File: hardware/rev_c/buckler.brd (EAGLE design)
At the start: 63.5 x 114.3 mm, 91 parts, among them J1 DB25_5747846, J2 DM3AT-SF-PEJM5, J7 NRF52832DK_SHIELD, U1 ADXL327, U2 MAX44009, U3 MPU-9250, U4 MS5637-02BA03, U5 SI7021-A20-GM1, U6 SIP32510

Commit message: Use actual parts instead of test points
Name nrf52dk headers too.
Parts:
- removed TP1, TP10, TP11, TP12, TP13, TP14, TP15, TP16, TP17, TP18, TP19, TP2, TP20, TP21, TP22, TP23, TP24, TP25, TP26, TP27, TP28, TP29, TP3, TP30, TP31, TP32, TP33, TP34, TP39, TP4, TP5, TP6, TP7, TP8, TP9: TEST_POINT_0.040IN, headers:TESTPOINT_0.040IN
- added JP1: (no value), SparkFun-Connectors:1X02
- added JP2: (no value), SparkFun-Connectors:1X04
- added JP3: (no value), SparkFun-Connectors:1X06
- added JP4: (no value), SparkFun-Connectors:1X08
- added JP5: M10", SparkFun-Connectors:1X10
- added JP6: (no value), SparkFun-Connectors:1X05
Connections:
- net !BUTTON_0: now also JP3.4; no longer TP26.TESTPOINT
- net !IMU_INTERRUPT: now also JP6.4; no longer TP1.TESTPOINT
- net !LCD_CS: now also JP4.8; no longer TP3.TESTPOINT
- net !LED_0: now also JP5.5; no longer TP5.TESTPOINT
- net !LED_1: now also JP5.6; no longer TP6.TESTPOINT
- net !LED_2: now also JP5.7; no longer TP7.TESTPOINT
- net !LIGHT_INTERRUPT: now also JP5.1; no longer TP2.TESTPOINT
- net !RESET: now also JP6.1; no longer TP39.TESTPOINT
- net !SD_CS: now also JP4.4; no longer TP4.TESTPOINT
- net +3V3: now also JP1.1, JP1.2, JP2.4; no longer TP28.TESTPOINT, TP29.TESTPOINT, TP30.TESTPOINT
- net +5V: now also JP2.3; no longer TP31.TESTPOINT
- net ANALOG_ACCEL_X: now also JP3.3; no longer TP10.TESTPOINT
- net ANALOG_ACCEL_Y: now also JP3.2; no longer TP11.TESTPOINT
- net ANALOG_ACCEL_Z: now also JP3.1; no longer TP12.TESTPOINT
- net GND: now also JP2.1, JP2.2, JP5.4; no longer TP32.TESTPOINT, TP33.TESTPOINT, TP34.TESTPOINT
- net GROVE_A0: now also JP3.5; no longer TP8.TESTPOINT
- net GROVE_A1: now also JP3.6; no longer TP9.TESTPOINT
- net GROVE_D0: now also JP5.3; no longer TP24.TESTPOINT
- net GROVE_D1: now also JP6.2; no longer TP19.TESTPOINT
- net LCD_MISO: now also JP4.6; no longer TP15.TESTPOINT
- net LCD_MOSI: now also JP4.5; no longer TP13.TESTPOINT
- net LCD_SCLK: now also JP4.7; no longer TP17.TESTPOINT
- net SD_ENABLE: now also JP5.2; no longer TP25.TESTPOINT
- net SD_MISO: now also JP4.2; no longer TP16.TESTPOINT
- net SD_MOSI: now also JP4.1; no longer TP14.TESTPOINT
- net SD_SCLK: now also JP4.3; no longer TP18.TESTPOINT
- net SENSORS_SCL: now also JP5.10; no longer TP20.TESTPOINT
- net SENSORS_SDA: now also JP5.9; no longer TP21.TESTPOINT
- net SWITCH_0: now also JP5.8; no longer TP27.TESTPOINT
- net UART_RX: now also JP6.5; no longer TP22.TESTPOINT
- net UART_TX: now also JP6.3; no longer TP23.TESTPOINT
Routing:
- net SENSORS_SCL: vias 7 -> 6
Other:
- board text added: "JP10"
- board text added: "JP11"
- board text added: "JP7"
- board text added: "JP8"
- board text added: "JP9"

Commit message: renumber headers
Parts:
- removed JP1: (no value), SparkFun-Connectors:1X02
- removed JP5: M10", SparkFun-Connectors:1X10
- added J13: (no value), headers:HW4-2.0
- added J16: DB25_5747846, headers:DB25_5747846
- J1: value DB25_5747846 -> NRF52832DK_SHIELD; device headers:DB25_5747846 -> headers:NRF52832DK_SHIELD
- J6: device headers:HW4-2.0 -> SparkFun-Connectors:1X02
- J7: value NRF52832DK_SHIELD -> M10"; device headers:NRF52832DK_SHIELD -> SparkFun-Connectors:1X10
- moved J1 89.1 mm to (7.62, 80.0), turned to 0 degrees
- moved J6 73.1 mm to (1.91, 77.5)
- moved J7 54.7 mm to (61.6, 89.2), turned to 270 degrees
- renumbered J2 to J17, J3 to J14, J4 to J15, J5 to J12, JP2 to J8, JP3 to J9, JP4 to J10, JP6 to J11
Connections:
- net !BUTTON_0: now also J1.P0.28; no longer J7.P0.28
- net !IMU_INTERRUPT: now also J1.P0.07; no longer J7.P0.07
- net !LCD_CS: now also J1.P0.18; no longer J7.P0.18
- net !LED_0: now also J1.P0.25, J7.5; no longer J7.P0.25, JP5.5
- net !LED_1: now also J1.P0.24, J7.6; no longer J7.P0.24, JP5.6
- net !LED_2: now also J1.P0.23, J7.7; no longer J7.P0.23, JP5.7
- net !LIGHT_INTERRUPT: now also J1.P0.27, J7.1; no longer J7.P0.27, JP5.1
- net !RESET: now also J1.P0.21; no longer J7.P0.21
- net !SD_CS: now also J1.P0.14; no longer J7.P0.14
- net +3V3: now also J1.3.3V@0, J1.3.3V@1, J1.3.3V@2, J13.3, J6.1, J6.2; no longer J6.3, J7.3.3V@0, J7.3.3V@1, J7.3.3V@2, JP1.1, JP1.2
- net +5V: now also J1.5V; no longer J7.5V
- net 5V_IN: now also J16.8, J16.9; no longer J1.8, J1.9
- net ANALOG_ACCEL_X: now also J1.P0.29; no longer J7.P0.29
- net ANALOG_ACCEL_Y: now also J1.P0.30; no longer J7.P0.30
- net ANALOG_ACCEL_Z: now also J1.P0.31; no longer J7.P0.31
- net GND: now also J1.GND@0, J1.GND@1, J1.GND@2, J13.4, J16.16, J16.20, J16.21, J16.24, J16.25, J16.6, J7.4; no longer J1.16, J1.20, J1.21, J1.24, J1.25, J1.6, J6.4, J7.GND@0, J7.GND@1, J7.GND@2, JP5.4
- net GROVE_A0: now also J1.P0.04; no longer J7.P0.04
- net GROVE_A1: now also J1.P0.03; no longer J7.P0.03
- net GROVE_D0: now also J1.P0.02, J13.1, J7.3; no longer J6.1, J7.P0.02, JP5.3
- net GROVE_D1: now also J1.P0.05, J13.2; no longer J6.2, J7.P0.05
- net LCD_MISO: now also J1.P0.16; no longer J7.P0.16
- net LCD_MOSI: now also J1.P0.15; no longer J7.P0.15
- net LCD_SCLK: now also J1.P0.17; no longer J7.P0.17
- net SD_ENABLE: now also J1.P0.26, J7.2; no longer J7.P0.26, JP5.2
- net SD_MISO: now also J1.P0.12; no longer J7.P0.12
- net SD_MOSI: now also J1.P0.11; no longer J7.P0.11
- net SD_SCLK: now also J1.P0.13; no longer J7.P0.13
- net SENSORS_SCL: now also J1.P0.19, J7.10; no longer J7.P0.19, JP5.10
- net SENSORS_SDA: now also J1.P0.20, J7.9; no longer J7.P0.20, JP5.9
- net SWITCH_0: now also J1.P0.22, J7.8; no longer J7.P0.22, JP5.8
- net UART_RX: now also J1.P0.08, J16.2; no longer J1.2, J7.P0.08
- net UART_TX: now also J1.P0.06, J16.1; no longer J1.1, J7.P0.06
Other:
- board text added: "J1"
- board text added: "J2"
- board text added: "J3"
- board text added: "J4"
- board text added: "J5"
- board text removed: "JP10"
- board text removed: "JP11"
- board text removed: "JP7"
- board text removed: "JP8"
- board text removed: "JP9"

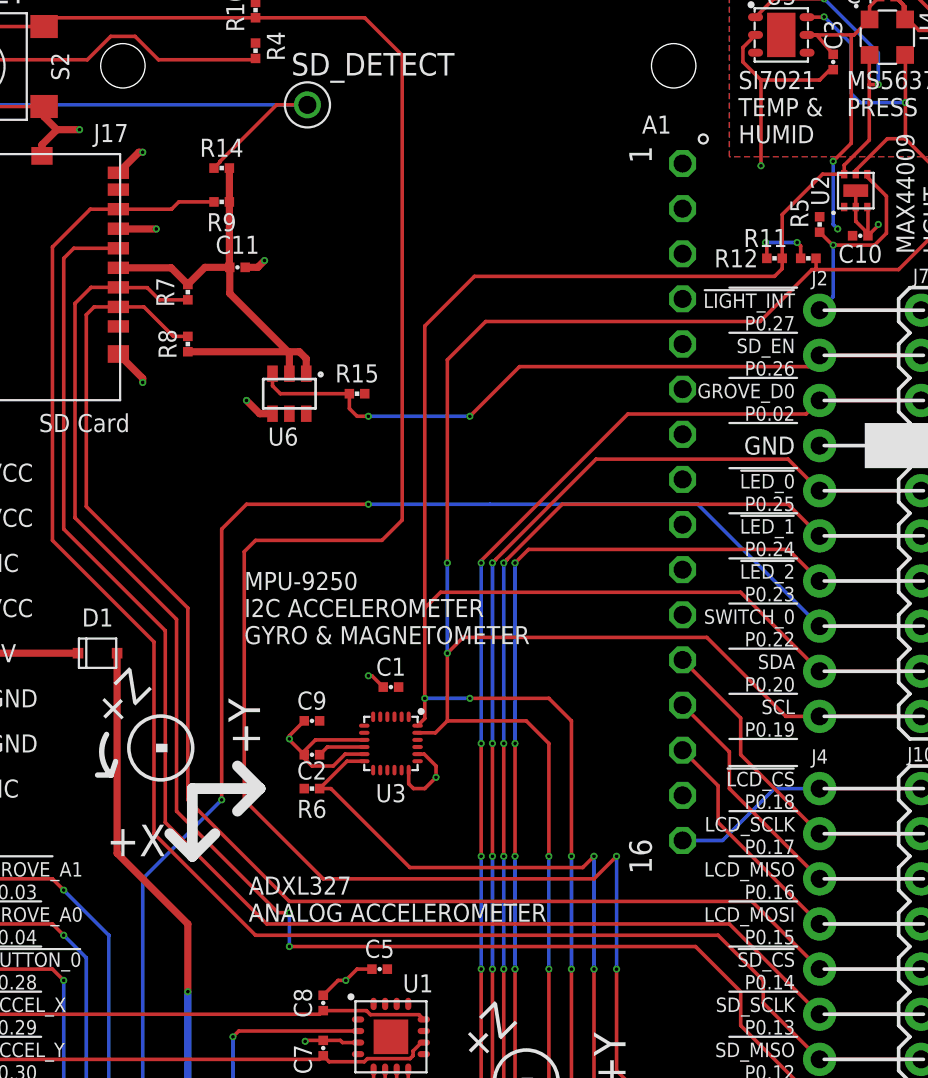
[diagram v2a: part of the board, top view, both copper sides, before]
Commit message: replace digital acc with lsm9ds1tr
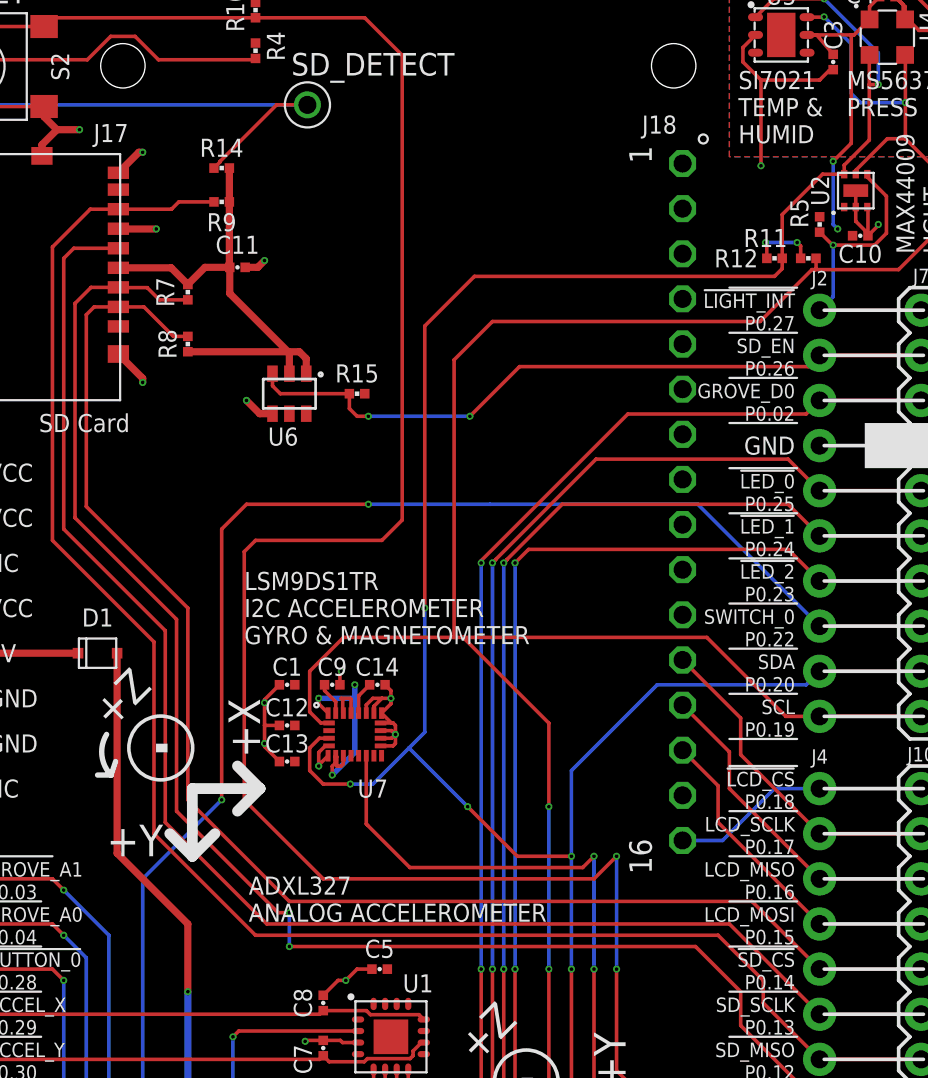
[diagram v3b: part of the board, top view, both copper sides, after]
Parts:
- removed C2: 100nF, passives:0402_CAP
- removed R6: 10k, passives:0402_RES
- removed U3: MPU-9250, chips:QFN-24/3MM
- added C12, C13: 100nF, passives:0402_CAP
- added C14: 10nF, passives:0402_CAP
- added U7: LSM9DS1TR, chips:LGA-24_3X3P5X1_STM
- moved C1 5.84 mm to (25.9, 68.1), turned to 0 degrees
- moved C9 2.33 mm to (28.4, 68.1), turned to 0 degrees
- renumbered A1 to J18
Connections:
- removed net N$19: C2.1, U3.10
- new net N$1: C9.1, U7.24
- new net N$6: C14.2, U7.21
- net !IMU_INTERRUPT: now also U7.11; no longer R6.1, U3.12
- net +3V3: now also C1.2, C12.2, C13.2, U7.1, U7.22, U7.23, U7.3, U7.7, U7.8; no longer C1.1, C9.1, R6.2, U3.1, U3.13, U3.22, U3.8
- net GND: now also C1.1, C12.1, C13.1, C14.1, U7.14, U7.15, U7.16, U7.17, U7.18, U7.19, U7.20, U7.5, U7.6; no longer C1.2, C2.2, U3.11, U3.18, U3.20, U3.9
- net SENSORS_SCL: now also U7.2; no longer U3.23
- net SENSORS_SDA: now also U7.4; no longer U3.24
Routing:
- net +3V3: track 33.2 -> 46.7 mm, vias 6 -> 9
- net SENSORS_SCL: track 170.6 -> 177.1 mm, vias 6 -> 4
- net GND: track 92.6 -> 95.9 mm, vias 20 -> 23
- net !IMU_INTERRUPT: track 60.2 -> 57.4 mm
- net SENSORS_SDA: track 166.1 -> 168.9 mm, vias 6 -> 7
- net N$19: track 2.69 -> 0.00 mm
- net N$1: track 0.00 -> 1.85 mm
- net N$6: track 0.00 -> 1.85 mm
- net GROVE_D0: vias 6 -> 4
- net !LED_2: vias 4 -> 2
- net !LED_1: vias 4 -> 2
- net !LED_0: vias 4 -> 2
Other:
- board text added: "LSM9DS1TR I2C ACCELEROMETER GYRO & MAGNETOMETER"
- board text removed: "MPU-9250 I2C ACCELEROMETER GYRO & MAGNETOMETER"

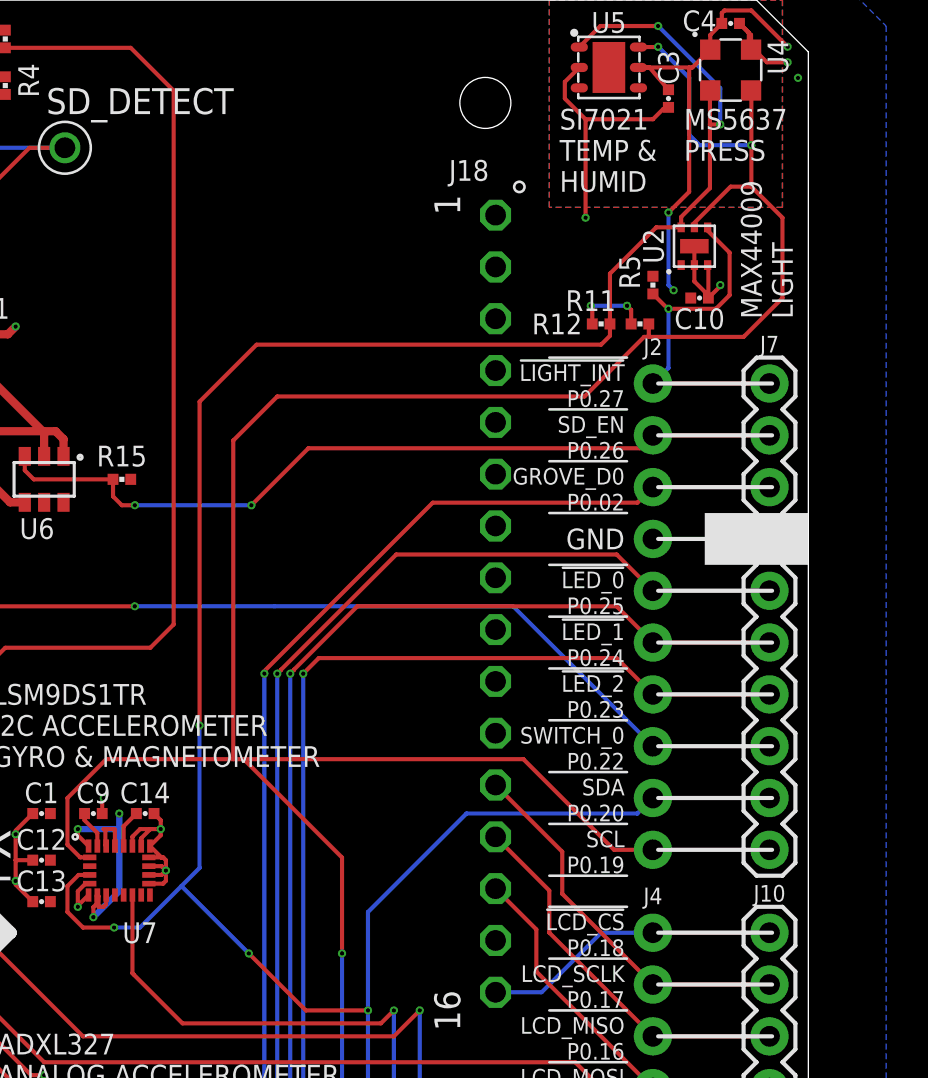
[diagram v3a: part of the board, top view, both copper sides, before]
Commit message: add OPT light sensor
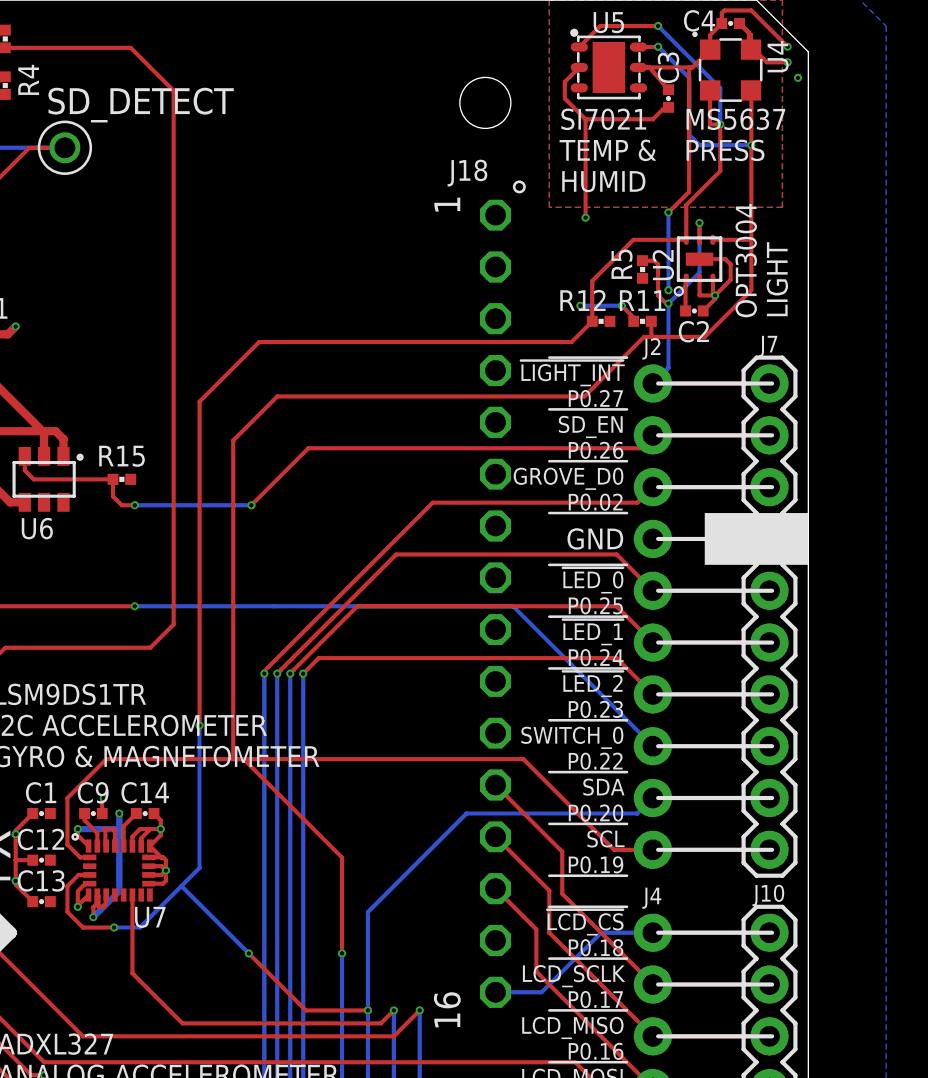
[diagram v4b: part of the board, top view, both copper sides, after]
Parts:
- removed C10: 1uF, passives:0402_CAP
- added C2: 100nF, passives:0402_CAP
- U2: value MAX44009 -> OPT3004DNPR; device chips:UDFN-6-EXPOSED -> chips:DNP0006A
- moved R5 0.92 mm to (55.4, 94.7), turned to 270 degrees
- moved U2 0.68 mm to (58.2, 95.2)
- moved R11 0.18 mm to (55.4, 92.2)
- moved R12 0.13 mm to (53.3, 92.2), turned to 0 degrees
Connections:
- net !LIGHT_INTERRUPT: now also U2.5; no longer U2.4
- net +3V3: now also C2.1; no longer C10.1
- net GND: now also C2.2, U2.7; no longer C10.2, U2.EP
- net SENSORS_SCL: now also U2.4; no longer U2.5
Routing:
- net SENSORS_SCL: track 177.1 -> 173.0 mm
- net GND: track 95.9 -> 97.6 mm
- net +3V3: track 46.7 -> 47.6 mm
- net !LIGHT_INTERRUPT: track 17.8 -> 18.4 mm, vias 1 -> 2
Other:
- board text added: "OPT3004 LIGHT"
- board text removed: "MAX44009 LIGHT"

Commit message: zip it up for quote
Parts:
- removed C14: 10nF, passives:0402_CAP
- removed R15: 100k, passives:0402_RES
- removed U7: LSM9DS1TR, chips:LGA-24_3X3P5X1_STM
- added C10: 100nF, passives:0402_CAP
- added R6: 10k, passives:0402_RES
- added U3: MS5637-02BA03, chips:4-SMD
- C11: value 4.7uF -> 100nF
- C13: value 100nF -> 4.7uF
- C2: value 100nF -> 10nF
- D3: value YELLOW -> GREEN
- D5: value GREEN -> YELLOW
- J10: device SparkFun-Connectors:1X08 -> SparkFun-Connectors:1X06
- J9: device SparkFun-Connectors:1X06 -> SparkFun-Connectors:1X08
- R13: value 10k -> 100k
- U2: value OPT3004DNPR -> LSM9DS1TR; device chips:DNP0006A -> chips:LGA-24_3X3P5X1_STM
- U4: value MS5637-02BA03 -> OPT3004DNPR; device chips:4-SMD -> chips:DNP0006A
- moved R12 77.4 mm to (12.1, 26.7)
- moved R13 71.2 mm to (22.2, 97.2)
- moved D3 70.9 mm to (3.30, 103.3), turned to 90 degrees
- moved D5 70.9 mm to (6.35, 32.4), turned to 0 degrees
- moved J10 59.7 mm to (1.91, 44.5)
- moved J9 59.7 mm to (61.6, 44.5)
- moved C12 41.8 mm to (57.9, 92.7)
- moved U2 41.3 mm to (29.7, 65.3), turned to 0 degrees
- moved C2 36.5 mm to (31.0, 68.1), turned to 180 degrees
- moved R10 34.2 mm to (55.4, 92.2), turned to 180 degrees
- moved C11 28.0 mm to (25.9, 63.8)
- moved C13 28.0 mm to (23.1, 91.6)
- moved R14 14.8 mm to (29.8, 84.5)
- moved R9 11.0 mm to (24.1, 106.0), turned to 90 degrees
- moved U4 9.40 mm to (58.2, 95.2), turned to 90 degrees
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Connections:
- net !BUTTON_0: now also J10.4, R12.1; no longer J9.4, R13.1
- net !IMU_INTERRUPT: now also U2.11; no longer U7.11
- net !LCD_CS: now also J9.8; no longer J10.8
- net !LED_1: now also D5.C; no longer D3.C
- net !LIGHT_INTERRUPT: now also U4.5; no longer U2.5
- net !RESET: now also R9.1; no longer R10.1
- net !SD_CS: now also J9.4, R7.1; no longer J10.4, R8.1
- net !SD_DETECT: now also R13.1; no longer R14.1
- net +3V3: now also C10.2, C11.2, C12.1, R14.2, R9.2, U2.22, U2.23, U2.3, U2.7, U2.8, U3.1; no longer C12.2, C13.2, C2.1, R13.2, R15.2, U7.1, U7.22, U7.23, U7.3, U7.7, U7.8
- net ANALOG_ACCEL_X: now also J10.3; no longer J9.3
- net ANALOG_ACCEL_Y: now also J10.2; no longer J9.2
- net ANALOG_ACCEL_Z: now also J10.1; no longer J9.1
- net GND: now also C10.1, C11.1, C12.2, C13.2, C2.1, D3.C, U2.14, U2.15, U2.16, U2.17, U2.18, U2.19, U2.20, U2.5, U2.6, U3.4, U4.2, U4.3, U4.7; no longer C11.2, C12.1, C13.1, C14.1, C2.2, D5.C, U2.2, U2.3, U2.7, U4.4, U7.14, U7.15, U7.16, U7.17, U7.18, U7.19, U7.20, U7.5, U7.6
- net GROVE_A0: now also J10.5; no longer J9.5
- net GROVE_A1: now also J10.6; no longer J9.6
- net LCD_MISO: now also J9.6; no longer J10.6
- net LCD_MOSI: now also J9.5; no longer J10.5
- net LCD_SCLK: now also J9.7; no longer J10.7
- net N$1: now also U2.24; no longer U7.24
- net N$18: now also C13.1, R13.2, R6.2; no longer C11.1, R14.2, R9.2
- net N$3: now also D3.A; no longer D5.A
- net N$5: now also D5.A; no longer D3.A
- net N$6: now also C2.2, U2.21; no longer C14.2, U7.21
- net SD_ENABLE: now also R14.1; no longer R15.1
- net SD_MISO: now also J9.2, R8.1; no longer J10.2, R9.1
- net SD_MOSI: now also J9.1, R6.1; no longer J10.1, R7.1
- net SD_SCLK: now also J9.3; no longer J10.3
- net SENSORS_SCL: now also R10.1, U2.2, U3.3, U4.4; no longer R11.1, U2.4, U4.3, U7.2
- net SENSORS_SDA: now also R11.1, U2.4, U3.2, U4.6; no longer R12.1, U2.6, U4.2, U7.4
